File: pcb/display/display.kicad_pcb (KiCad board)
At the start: 2 copper layers, 86 x 64 mm, 18 parts, among them J1 Conn_01x08, U1 EA_DOGL128X-6

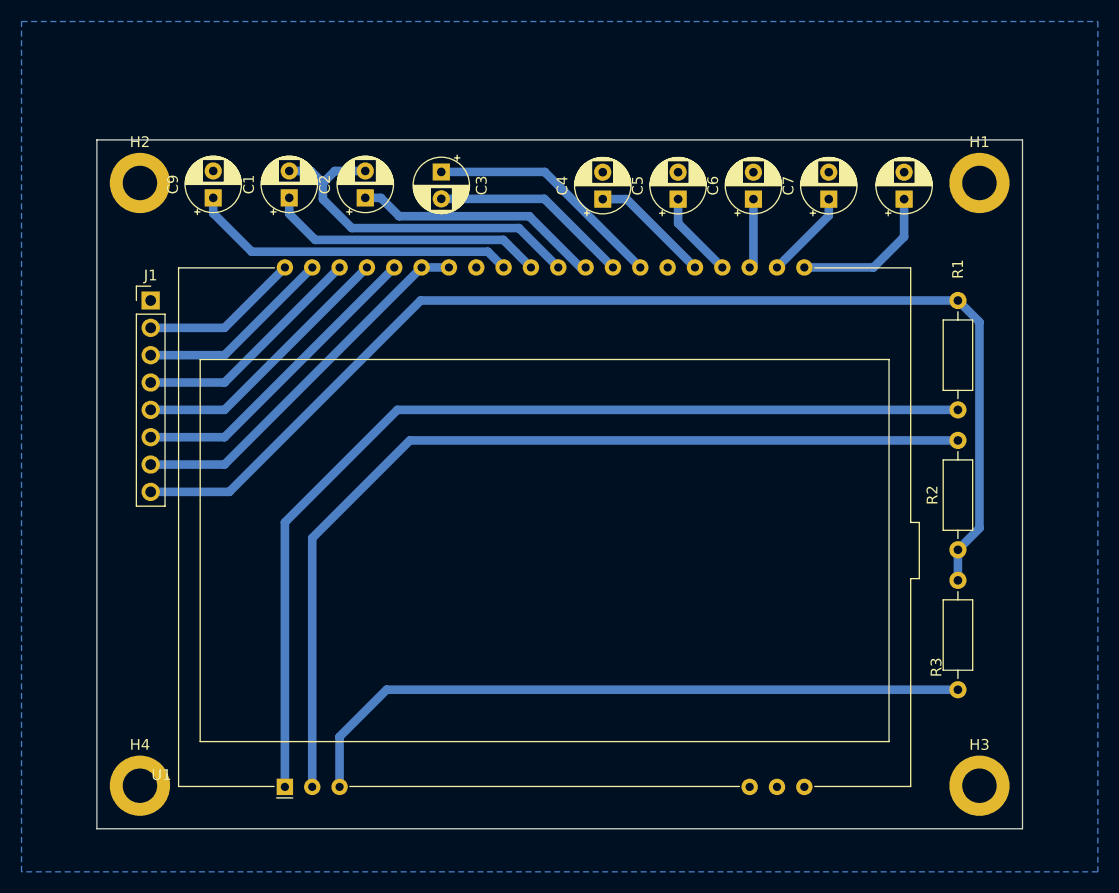
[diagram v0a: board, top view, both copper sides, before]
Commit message: resize display pcb to match main board
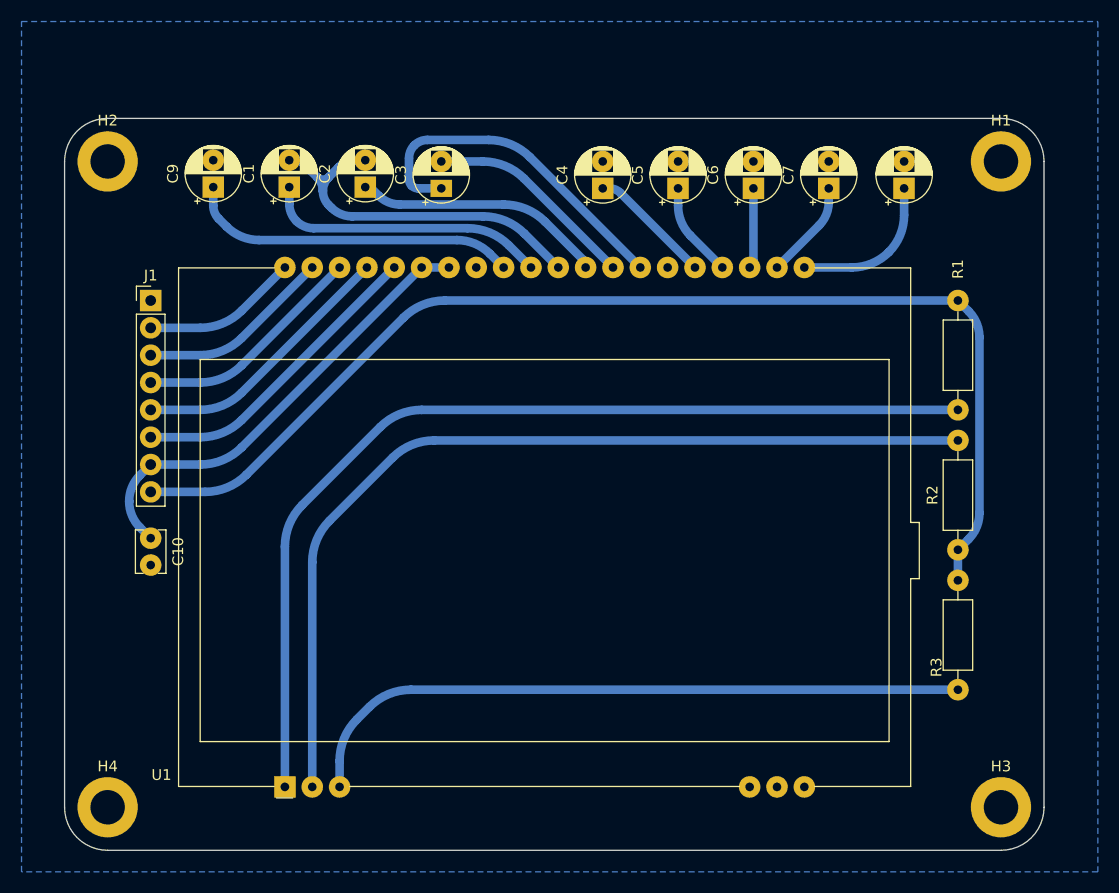
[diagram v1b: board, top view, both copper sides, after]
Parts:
- added C10: 10nF, Capacitor_THT:C_Disc_D3.8mm_W2.6mm_P2.50mm, F.Cu at (100.0, 94.0)
- moved H2 3.61 mm to (96.0, 59.0)
- moved H4 3.61 mm to (96.0, 119.0)
- moved H1 2.83 mm to (179.0, 59.0)
- moved H3 2.83 mm to (179.0, 119.0)
- moved C3 1.53 mm to (127.0, 61.5), turned to 90 degrees
- moved C1 1.00 mm to (112.9, 61.4)
- moved C2 1.00 mm to (119.9, 61.4)
- moved C4 1.00 mm to (142.0, 61.5)
- moved C5 1.00 mm to (149.0, 61.5)
- moved C6 1.00 mm to (156.0, 61.5)
- moved C7 1.00 mm to (163.0, 61.5)
- moved C8 1.00 mm to (170.0, 61.5)
- moved C9 1.00 mm to (105.8, 61.4)
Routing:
- net Net-(U1-CAP2N): track 22.2 -> 32.5 mm
- net +3.3V: track 35.3 -> 43.2 mm
- net Net-(U1-CAP1N): track 34.0 -> 35.9 mm
- net Net-(U1-CAP2P): track 18.6 -> 19.8 mm
- net Net-(U1-V2): track 6.49 -> 7.47 mm
- net Net-(U1-V1): track 8.34 -> 9.19 mm
- net +5V: track 110.0 -> 109.2 mm
- net Net-(U1-V3): track 8.05 -> 8.86 mm
- net Net-(U1-V0): track 14.0 -> 14.5 mm
- net Net-(U1-A2+): track 86.9 -> 86.3 mm
- net Net-(U1-A1+): track 91.4 -> 90.9 mm
- net Net-(U1-A3+): track 63.9 -> 63.4 mm
- net Net-(U1-CAP3P): track 26.0 -> 26.5 mm
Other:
- board size 86 x 64 mm -> 91 x 68 mm
